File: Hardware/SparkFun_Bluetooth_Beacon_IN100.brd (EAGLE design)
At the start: 25.4 x 25.4 mm, 62 parts, among them J3 Vertical Qwiic Connector, U1 IN100, Y1 CRYSTAL-26MHZSMD-3.2X2.5

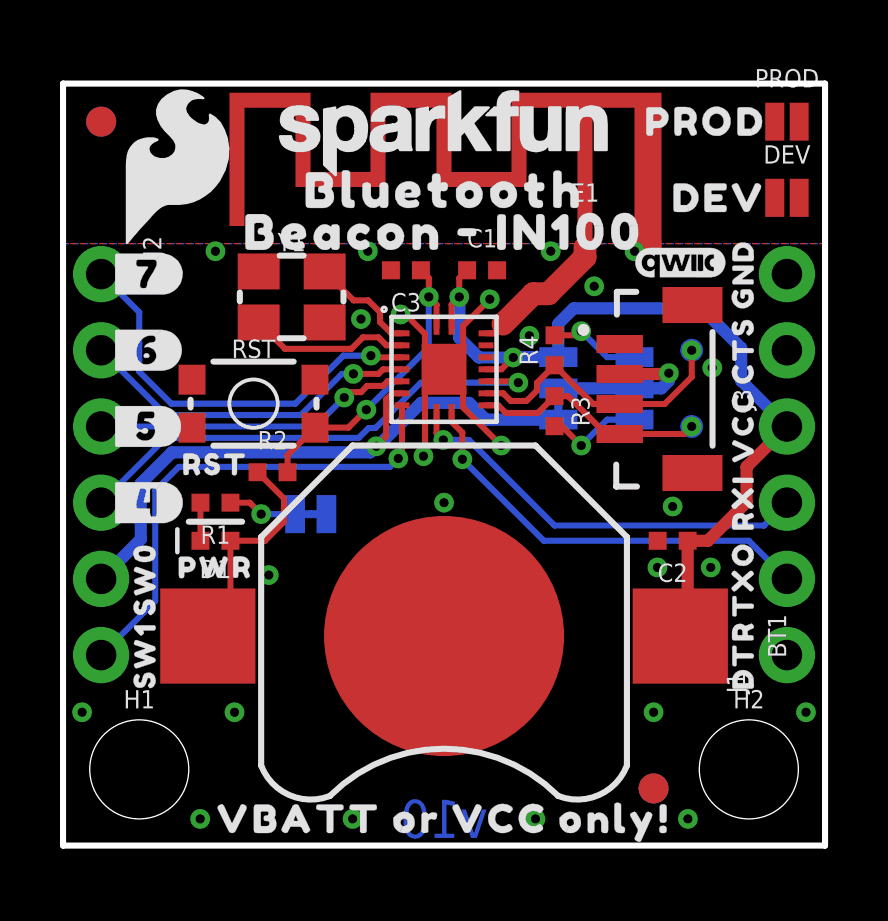
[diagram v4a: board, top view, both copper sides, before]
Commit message: Design review updates
Improve GND continuity
Add some small restrict regions to improve copper pour
Nudge "PROD" and "DEV" text away from pads
In schematic, move reset button to near main IC, and replace with Product Identifier pads
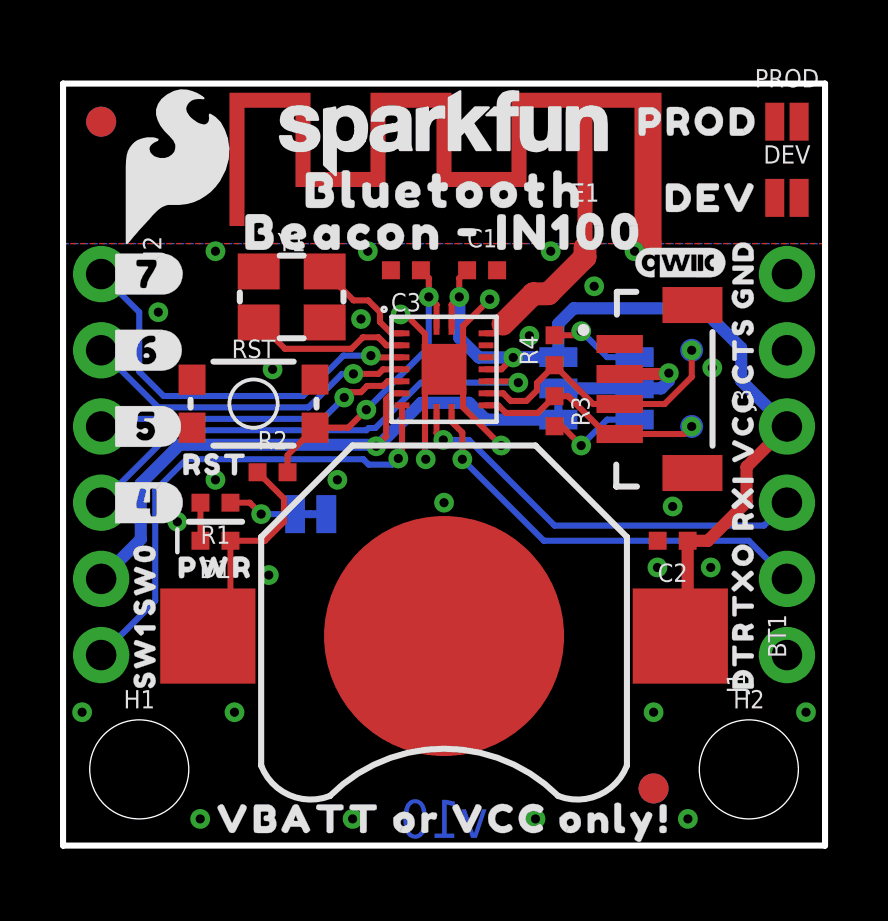
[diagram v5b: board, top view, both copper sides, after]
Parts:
- moved U$28 0.25 mm to (23.9, 21.6)
- moved U$29 0.25 mm to (23.9, 24.1)
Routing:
- net GND: track 12.0 -> 12.1 mm, vias 25 -> 30
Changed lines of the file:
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@@
 <dimension x1="0" y1="0" x2="0" y2="6.985" x3="-1.27" y3="3.4925" textsize="1.778" textratio="15" layer="47" unit="inch" precision="3"/>
 <wire x1="4.191" y1="10.795" x2="5.969" y2="10.795" width="0.2032" layer="21"/>
+<rectangle x1="10.795" y1="16.256" x2="11.557" y2="16.383" layer="42"/>
+<rectangle x1="11.684" y1="16.764" x2="11.811" y2="16.891" layer="41"/>
+<rectangle x1="13.589" y1="16.764" x2="13.716" y2="16.891" layer="41"/>
+<rectangle x1="11.684" y1="14.859" x2="11.811" y2="14.986" layer="41"/>
+<rectangle x1="13.589" y1="14.859" x2="13.716" y2="14.986" layer="41"/>
 </plain>
 <attributes>
@@
 <element name="U$23" library="output" package="RST0" value="" x="5.08" y="12.7" smashed="yes"/>
 <element name="LOGO3" library="SparkFun-Aesthetics" package="QWIIC_3MM" value="QWIIC_LOGO_3MM" x="20.574" y="19.431" smashed="yes"/>
-<element name="U$28" library="output" package="DEV0" value="" x="24.13" y="21.59" smashed="yes"/>
-<element name="U$29" library="output" package="PROD0" value="" x="24.13" y="24.13" smashed="yes"/>
+<element name="U$28" library="output" package="DEV0" value="" x="23.876" y="21.59" smashed="yes"/>
+<element name="U$29" library="output" package="PROD0" value="" x="23.876" y="24.13" smashed="yes"/>
 <element name="PROD" library="SparkFun-Jumpers" package="SMT-JUMPER_2_NC_PASTE_NO-SILK" package3d_urn="urn:adsk.eagle:package:39283/1" value="JUMPER-SMT_2_NC_PASTE_NO-SILK" x="24.13" y="24.13" smashed="yes">
 <attribute name="NAME" x="24.13" y="25.273" size="0.6096" layer="25" font="vector" ratio="20" align="bottom-center"/>
@@
 <wire x1="12.065" y1="16.51" x2="12.065" y2="17.05513125" width="0.2032" layer="1"/>
 <wire x1="12.7" y1="15.875" x2="12.065" y2="15.24" width="0.2032" layer="1"/>
-<wire x1="12.065" y1="13.0302" x2="12.065" y2="15.24" width="0.2032" layer="1"/>
+<wire x1="12.0904" y1="12.8778" x2="12.065" y2="12.9032" width="0.2032" layer="1"/>
+<wire x1="12.065" y1="15.24" x2="12.065" y2="12.9032" width="0.2032" layer="1"/>
 <wire x1="12.7" y1="15.875" x2="13.335" y2="15.24" width="0.2032" layer="1"/>
 <wire x1="13.335" y1="14.605" x2="13.335" y2="15.24" width="0.2032" layer="1"/>
-<via x="12.0142" y="12.9794" extent="1-16" drill="0.3048"/>
-<wire x1="12.065" y1="13.0302" x2="12.0142" y2="12.9794" width="0.2032" layer="1"/>
+<via x="12.0904" y="12.8778" extent="1-16" drill="0.3048"/>
 <via x="10.16" y="19.812" extent="1-16" drill="0.3048"/>
 <via x="5.08" y="19.812" extent="1-16" drill="0.3048"/>
@@
 <contactref element="RST" pad="3"/>
 <via x="9.9314" y="17.5514" extent="1-16" drill="0.3048"/>
+<via x="6.985" y="15.875" extent="1-16" drill="0.3048"/>
+<via x="5.08" y="12.192" extent="1-16" drill="0.3048"/>
+<via x="3.81" y="10.795" extent="1-16" drill="0.3048"/>
+<via x="9.144" y="12.192" extent="1-16" drill="0.3048"/>
+<via x="3.175" y="17.78" extent="1-16" drill="0.3048"/>
 </signal>
 <signal name="N$4">
@@
 <wire x1="10.9698" y1="15.075" x2="10.7706" y2="14.8758" width="0.2032" layer="1"/>
 <via x="10.4404" y="13.3096" extent="1-16" drill="0.3048"/>
-<wire x1="10.4404" y1="13.3096" x2="10.2372" y2="13.1064" width="0.4064" layer="16"/>
-<wire x1="10.2372" y1="13.1064" x2="3.6322" y2="13.1064" width="0.4064" layer="16"/>
+<wire x1="10.4404" y1="13.3096" x2="10.3896" y2="13.3604" width="0.4064" layer="16"/>
+<wire x1="10.3896" y1="13.3604" x2="3.8862" y2="13.3604" width="0.4064" layer="16"/>
 <wire x1="1.27" y1="8.89" x2="2.5908" y2="10.2108" width="0.4064" layer="16"/>
 <wire x1="2.5908" y1="10.2108" x2="2.5908" y2="12.065" width="0.4064" layer="16"/>
-<wire x1="2.5908" y1="12.065" x2="3.6322" y2="13.1064" width="0.4064" layer="16"/>
+<wire x1="2.5908" y1="12.065" x2="3.8862" y2="13.3604" width="0.4064" layer="16"/>
 <wire x1="16.51" y1="14.1986" x2="14.097" y2="14.1986" width="0.4064" layer="16"/>
 <wire x1="14.097" y1="14.1986" x2="13.5382" y2="14.7574" width="0.4064" layer="16"/>
@@
 <wire x1="11.3" y1="14.675" x2="11.3" y2="13.0272" width="0.2032" layer="1"/>
 <via x="11.176" y="12.9032" extent="1-16" drill="0.3048"/>
-<wire x1="11.176" y1="12.9032" x2="10.8966" y2="12.6238" width="0.2032" layer="16"/>
 <wire x1="1.27" y1="6.35" x2="3.0734" y2="8.1534" width="0.2032" layer="16"/>
 <wire x1="3.0734" y1="8.1534" x2="3.0734" y2="11.8364" width="0.2032" layer="16"/>
-<wire x1="3.0734" y1="11.8364" x2="3.8608" y2="12.6238" width="0.2032" layer="16"/>
-<wire x1="3.8608" y1="12.6238" x2="10.8966" y2="12.6238" width="0.2032" layer="16"/>
+<wire x1="3.0734" y1="11.8364" x2="4.1148" y2="12.8778" width="0.2032" layer="16"/>
+<wire x1="4.1148" y1="12.8778" x2="10.01009375" y2="12.8778" width="0.2032" layer="16"/>
+<wire x1="11.176" y1="12.9032" x2="10.9728" y2="12.7" width="0.2032" layer="16"/>
+<wire x1="10.18789375" y1="12.7" x2="10.01009375" y2="12.8778" width="0.2032" layer="16"/>
+<wire x1="10.9728" y1="12.7" x2="10.18789375" y2="12.7" width="0.2032" layer="16"/>
 </signal>
 <signal name="IO4">
@@
 <wire x1="15.175753125" y1="15.431246875" x2="11.926046875" y2="15.431246875" width="0.2032" layer="16"/>
 <wire x1="10.414" y1="13.9192" x2="11.926046875" y2="15.431246875" width="0.2032" layer="16"/>
-<wire x1="1.27" y1="11.43" x2="3.429" y2="13.589" width="0.2032" layer="16"/>
-<wire x1="3.429" y1="13.589" x2="9.8552" y2="13.589" width="0.2032" layer="16"/>
-<wire x1="9.8552" y1="13.589" x2="10.1854" y2="13.9192" width="0.2032" layer="16"/>
+<wire x1="1.27" y1="11.43" x2="3.683" y2="13.843" width="0.2032" layer="16"/>
+<wire x1="3.683" y1="13.843" x2="10.1092" y2="13.843" width="0.2032" layer="16"/>
+<wire x1="10.1092" y1="13.843" x2="10.1854" y2="13.9192" width="0.2032" layer="16"/>
 <wire x1="10.1854" y1="13.9192" x2="10.414" y2="13.9192" width="0.2032" layer="16"/>
 </signal>
@@
 <wire x1="9.5504" y1="15.113" x2="9.3726" y2="14.9352" width="0.2032" layer="1"/>
 <via x="9.3726" y="14.9352" extent="1-16" drill="0.3048"/>
-<wire x1="9.3726" y1="14.9352" x2="8.4074" y2="13.97" width="0.2032" layer="16"/>
-<wire x1="8.4074" y1="13.97" x2="1.27" y2="13.97" width="0.2032" layer="16"/>
+<wire x1="9.3726" y1="14.9352" x2="8.6614" y2="14.224" width="0.2032" layer="16"/>
+<wire x1="8.6614" y1="14.224" x2="1.524" y2="14.224" width="0.2032" layer="16"/>
+<wire x1="1.524" y1="14.224" x2="1.27" y2="13.97" width="0.2032" layer="16"/>
 </signal>
 <signal name="IO6">
@@
 <via x="9.6774" y="15.7226" extent="1-16" drill="0.3048"/>
 <wire x1="9.6774" y1="15.7226" x2="9.2964" y2="15.7226" width="0.2032" layer="16"/>
-<wire x1="9.2964" y1="15.7226" x2="7.9248" y2="14.351" width="0.2032" layer="16"/>
-<wire x1="7.9248" y1="14.351" x2="3.429" y2="14.351" width="0.2032" layer="16"/>
-<wire x1="3.429" y1="14.351" x2="1.27" y2="16.51" width="0.2032" layer="16"/>
+<wire x1="9.2964" y1="15.7226" x2="8.1788" y2="14.605" width="0.2032" layer="16"/>
+<wire x1="8.1788" y1="14.605" x2="3.175" y2="14.605" width="0.2032" layer="16"/>
+<wire x1="3.175" y1="14.605" x2="1.27" y2="16.51" width="0.2032" layer="16"/>
 </signal>
 <signal name="IO7">
@@
 <via x="10.2616" y="16.3322" extent="1-16" drill="0.3048"/>
 <wire x1="10.2616" y1="16.3322" x2="9.3472" y2="16.3322" width="0.2032" layer="16"/>
-<wire x1="7.747" y1="14.732" x2="9.3472" y2="16.3322" width="0.2032" layer="16"/>
+<wire x1="8.001" y1="14.986" x2="9.3472" y2="16.3322" width="0.2032" layer="16"/>
 <wire x1="1.27" y1="19.05" x2="2.54" y2="17.78" width="0.2032" layer="16"/>
 <wire x1="2.54" y1="17.78" x2="2.54" y2="15.7988" width="0.2032" layer="16"/>
-<wire x1="2.54" y1="15.7988" x2="3.6068" y2="14.732" width="0.2032" layer="16"/>
-<wire x1="3.6068" y1="14.732" x2="7.747" y2="14.732" width="0.2032" layer="16"/>
+<wire x1="2.54" y1="15.7988" x2="3.3528" y2="14.986" width="0.2032" layer="16"/>
+<wire x1="3.3528" y1="14.986" x2="8.001" y2="14.986" width="0.2032" layer="16"/>
 </signal>
 <signal name="SCL/IO2">

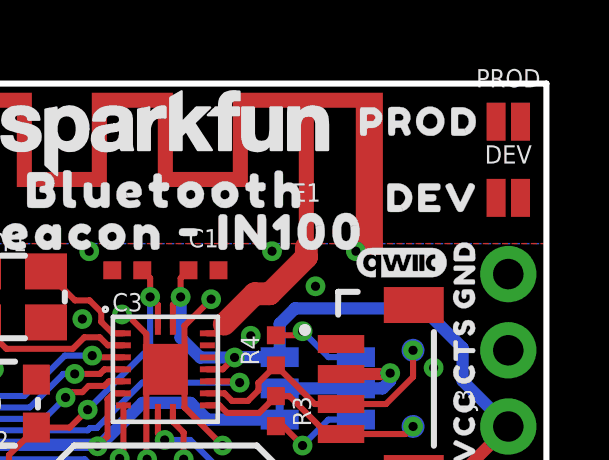
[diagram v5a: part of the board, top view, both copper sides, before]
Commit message: Change identifier pads to solid versions
Also approve extraneous DRC jumper overlap error
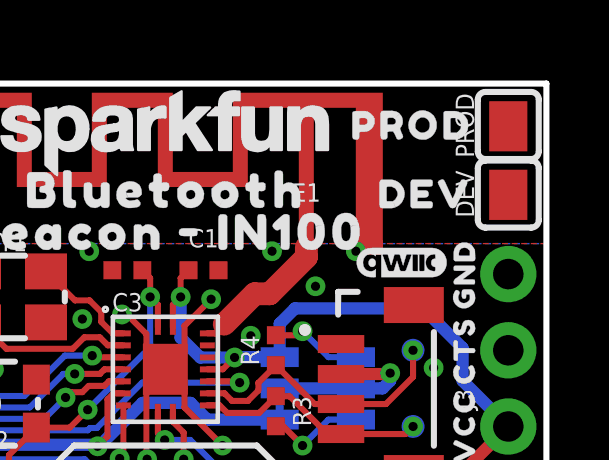
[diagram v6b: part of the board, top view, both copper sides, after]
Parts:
- DEV, PROD: value JUMPER-SMT_2_NC_PASTE_NO-SILK -> PROD_ID_PASTE_SILK; device SparkFun-Jumpers:SMT-JUMPER_2_NC_PASTE_NO-SILK -> SparkFun-Aesthetics:PRODUCT_IDENT_PASTE_SILK
- moved U$28 0.28 mm to (23.6, 21.7)
- moved U$29 0.28 mm to (23.6, 24.0)
- moved DEV 0.13 mm to (24.1, 21.7), turned to 90 degrees
- moved PROD 0.13 mm to (24.1, 24.0), turned to 90 degrees
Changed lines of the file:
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@@
 <element name="U$23" library="output" package="RST0" value="" x="5.08" y="12.7" smashed="yes"/>
 <element name="LOGO3" library="SparkFun-Aesthetics" package="QWIIC_3MM" value="QWIIC_LOGO_3MM" x="20.574" y="19.431" smashed="yes"/>
-<element name="U$28" library="output" package="DEV0" value="" x="23.876" y="21.59" smashed="yes"/>
-<element name="U$29" library="output" package="PROD0" value="" x="23.876" y="24.13" smashed="yes"/>
-<element name="PROD" library="SparkFun-Jumpers" package="SMT-JUMPER_2_NC_PASTE_NO-SILK" package3d_urn="urn:adsk.eagle:package:39283/1" value="JUMPER-SMT_2_NC_PASTE_NO-SILK" x="24.13" y="24.13" smashed="yes">
-<attribute name="NAME" x="24.13" y="25.273" size="0.6096" layer="25" font="vector" ratio="20" align="bottom-center"/>
-<attribute name="VALUE" x="24.13" y="22.987" size="0.6096" layer="27" font="vector" ratio="20" align="top-center"/>
+<element name="U$28" library="output" package="DEV0" value="" x="23.622" y="21.717" smashed="yes"/>
+<element name="U$29" library="output" package="PROD0" value="" x="23.622" y="24.003" smashed="yes"/>
+<element name="PROD" library="SparkFun-Aesthetics" package="PRODUCT_IDENT_PASTE_SILK" value="PROD_ID_PASTE_SILK" x="24.13" y="24.003" smashed="yes" rot="R90">
+<attribute name="NAME" x="22.987" y="24.003" size="0.6096" layer="25" font="vector" ratio="20" rot="R90" align="bottom-center"/>
+<attribute name="VALUE" x="25.273" y="24.003" size="0.6096" layer="27" font="vector" ratio="20" rot="R90" align="top-center"/>
 </element>
-<element name="DEV" library="SparkFun-Jumpers" package="SMT-JUMPER_2_NC_PASTE_NO-SILK" package3d_urn="urn:adsk.eagle:package:39283/1" value="JUMPER-SMT_2_NC_PASTE_NO-SILK" x="24.13" y="21.59" smashed="yes">
-<attribute name="NAME" x="24.13" y="22.733" size="0.6096" layer="25" font="vector" ratio="20" align="bottom-center"/>
-<attribute name="VALUE" x="24.13" y="20.447" size="0.6096" layer="27" font="vector" ratio="20" align="top-center"/>
+<element name="DEV" library="SparkFun-Aesthetics" package="PRODUCT_IDENT_PASTE_SILK" value="PROD_ID_PASTE_SILK" x="24.13" y="21.717" smashed="yes" rot="R90">
+<attribute name="NAME" x="22.987" y="21.717" size="0.6096" layer="25" font="vector" ratio="20" rot="R90" align="bottom-center"/>
+<attribute name="VALUE" x="25.273" y="21.717" size="0.6096" layer="27" font="vector" ratio="20" rot="R90" align="top-center"/>
 </element>
 </elements>

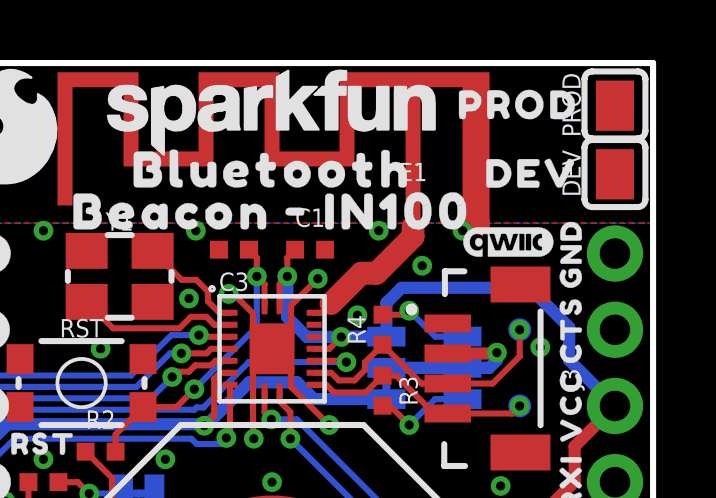
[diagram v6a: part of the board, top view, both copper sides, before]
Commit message: Checklist updates
Add PROD_ID to IN100 device
Add name and value to IN100 footprint
Add selective solder paths to layer 48
Move product identifier pads out of selective solder path
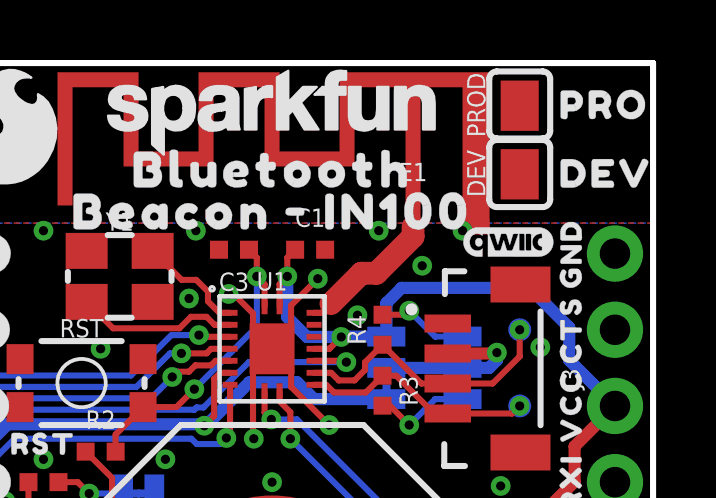
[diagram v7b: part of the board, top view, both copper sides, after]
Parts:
- removed U$29: (no value), output:PROD0
- added U$30: (no value), output:PRO0
- moved DEV 3.18 mm to (21.0, 21.7)
- moved PROD 3.18 mm to (21.0, 24.0)
- moved U$28 2.03 mm to (21.6, 21.7)
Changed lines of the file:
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@@
 <rectangle x1="11.684" y1="14.859" x2="11.811" y2="14.986" layer="41"/>
 <rectangle x1="13.589" y1="14.859" x2="13.716" y2="14.986" layer="41"/>
+<wire x1="25.4" y1="25.4" x2="25.4" y2="0" width="4.5212" layer="48"/>
+<wire x1="0" y1="25.4" x2="0" y2="0" width="4.5212" layer="48"/>
 </plain>
 <attributes>
@@
 <attribute name="REV" value="" x="-10.16" y="-25.4" size="1.778" layer="27" font="vector" ratio="15" display="off"/>
 </element>
-<element name="U1" library="IN100" package="IN100" value="IN100" x="12.7" y="15.875" smashed="yes"/>
+<element name="U1" library="IN100" package="IN100" value="IN100" x="12.7" y="15.875" smashed="yes">
+<attribute name="NAME" x="12.7" y="18.125" size="0.6096" layer="25" font="vector" ratio="20" align="center"/>
+<attribute name="PROD_ID" value="IC-17260" x="12.7" y="15.875" size="1.778" layer="27" display="off"/>
+<attribute name="VALUE" x="12.7" y="13.625" size="0.6096" layer="27" font="vector" ratio="20" align="center"/>
+</element>
 <element name="Y1" library="SparkFun-Clocks" package="CRYSTAL-SMD-3.2X2.5MM" value="CRYSTAL-26MHZSMD-3.2X2.5" x="7.62" y="18.288" smashed="yes">
 <attribute name="NAME" x="7.62" y="19.812" size="0.6096" layer="25" font="vector" ratio="20" align="bottom-center"/>
@@
 <element name="U$23" library="output" package="RST0" value="" x="5.08" y="12.7" smashed="yes"/>
 <element name="LOGO3" library="SparkFun-Aesthetics" package="QWIIC_3MM" value="QWIIC_LOGO_3MM" x="20.574" y="19.431" smashed="yes"/>
-<element name="U$28" library="output" package="DEV0" value="" x="23.622" y="21.717" smashed="yes"/>
-<element name="U$29" library="output" package="PROD0" value="" x="23.622" y="24.003" smashed="yes"/>
-<element name="PROD" library="SparkFun-Aesthetics" package="PRODUCT_IDENT_PASTE_SILK" value="PROD_ID_PASTE_SILK" x="24.13" y="24.003" smashed="yes" rot="R90">
-<attribute name="NAME" x="22.987" y="24.003" size="0.6096" layer="25" font="vector" ratio="20" rot="R90" align="bottom-center"/>
-<attribute name="VALUE" x="25.273" y="24.003" size="0.6096" layer="27" font="vector" ratio="20" rot="R90" align="top-center"/>
-</element>
-<element name="DEV" library="SparkFun-Aesthetics" package="PRODUCT_IDENT_PASTE_SILK" value="PROD_ID_PASTE_SILK" x="24.13" y="21.717" smashed="yes" rot="R90">
-<attribute name="NAME" x="22.987" y="21.717" size="0.6096" layer="25" font="vector" ratio="20" rot="R90" align="bottom-center"/>
-<attribute name="VALUE" x="25.273" y="21.717" size="0.6096" layer="27" font="vector" ratio="20" rot="R90" align="top-center"/>
-</element>
+<element name="U$28" library="output" package="DEV0" value="" x="21.59" y="21.717" smashed="yes"/>
+<element name="PROD" library="SparkFun-Aesthetics" package="PRODUCT_IDENT_PASTE_SILK" value="PROD_ID_PASTE_SILK" x="20.955" y="24.003" smashed="yes" rot="R90">
+<attribute name="NAME" x="19.812" y="24.003" size="0.6096" layer="25" font="vector" ratio="20" rot="R90" align="bottom-center"/>
+<attribute name="VALUE" x="22.098" y="24.003" size="0.6096" layer="27" font="vector" ratio="20" rot="R90" align="top-center"/>
+</element>
+<element name="DEV" library="SparkFun-Aesthetics" package="PRODUCT_IDENT_PASTE_SILK" value="PROD_ID_PASTE_SILK" x="20.955" y="21.717" smashed="yes" rot="R90">
+<attribute name="NAME" x="19.812" y="21.717" size="0.6096" layer="25" font="vector" ratio="20" rot="R90" align="bottom-center"/>
+<attribute name="VALUE" x="22.098" y="21.717" size="0.6096" layer="27" font="vector" ratio="20" rot="R90" align="top-center"/>
+</element>
+<element name="U$30" library="output" package="PRO0" value="" x="21.59" y="24.003" smashed="yes"/>
 </elements>
 <signals>
